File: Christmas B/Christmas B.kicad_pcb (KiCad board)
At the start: 2 copper layers, 80.1 x 92.6 mm, 38 parts, among them J1 LEFT, J2 RIGHT

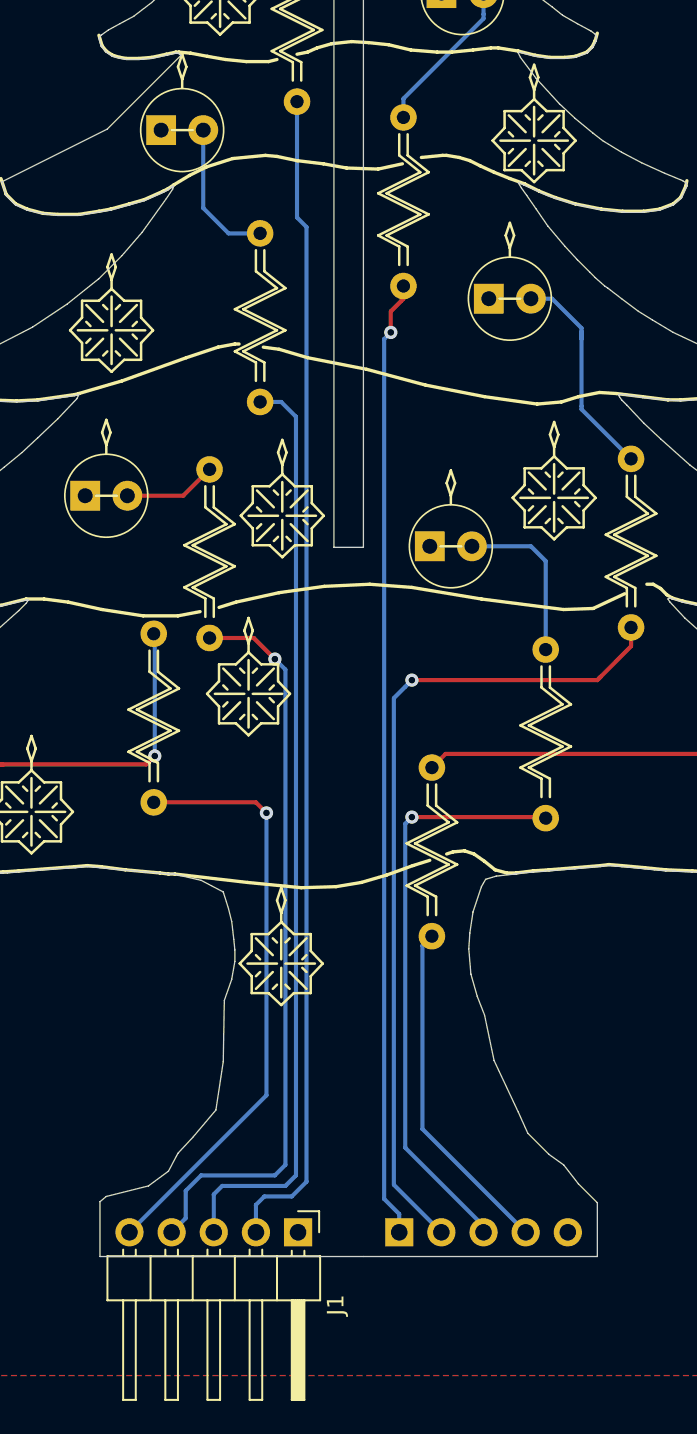
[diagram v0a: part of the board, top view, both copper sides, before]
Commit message: Make space at the bottom
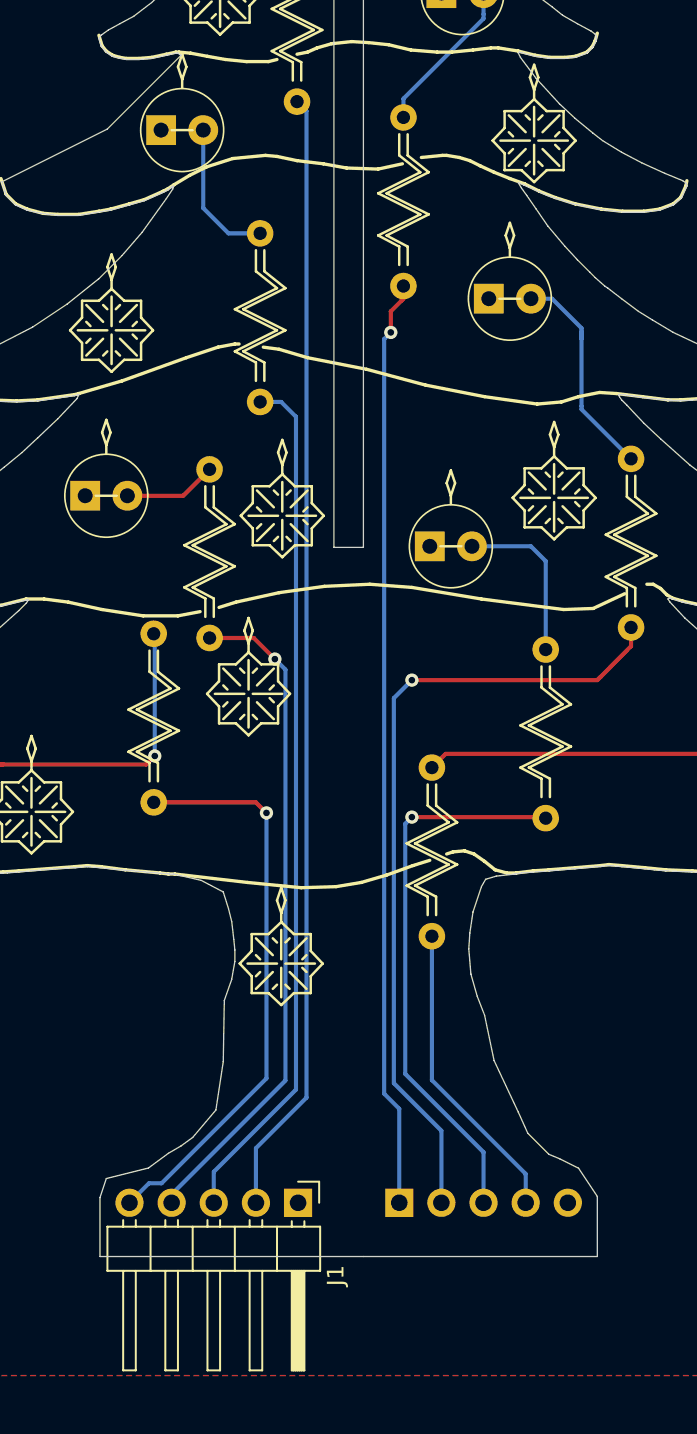
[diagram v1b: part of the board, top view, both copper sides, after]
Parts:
- moved J1 1.78 mm to (101.7, 148.3)
- moved J2 1.78 mm to (107.8, 148.3)
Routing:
- net Net-(J1-Pad4): track 44.7 -> 40.3 mm
- net Net-(J1-Pad3): track 56.0 -> 51.9 mm
- net Net-(J1-Pad2): track 70.6 -> 67.9 mm
- net Net-(J2-Pad4): track 20.7 -> 18.4 mm
- net Net-(J2-Pad3): track 35.2 -> 33.5 mm
- net Net-(J2-Pad2): track 50.3 -> 48.5 mm
- net Net-(J2-Pad1): track 57.9 -> 56.1 mm
- net Net-(J1-Pad5): track 35.7 -> 34.4 mm
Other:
- outline, holes or cut-outs redrawn

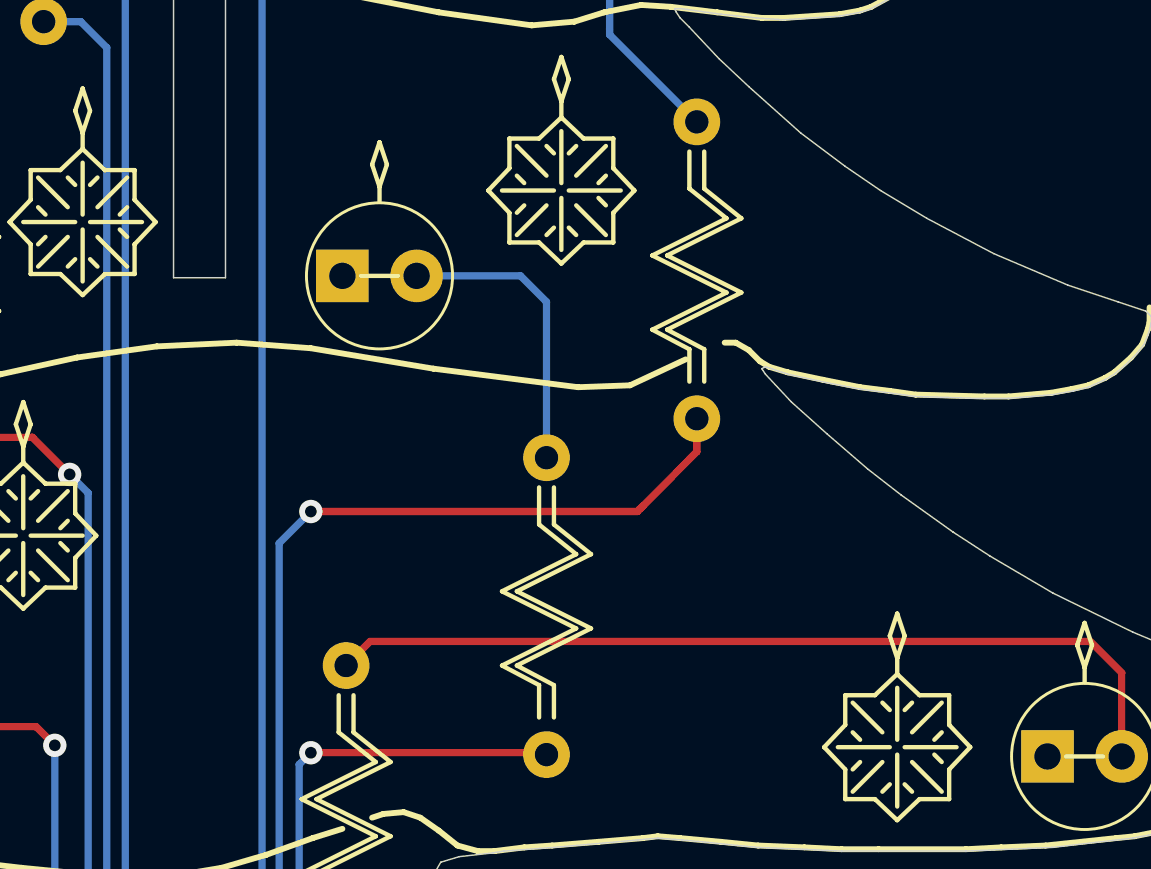
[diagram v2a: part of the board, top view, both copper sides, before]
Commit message: Added part designation to A/B
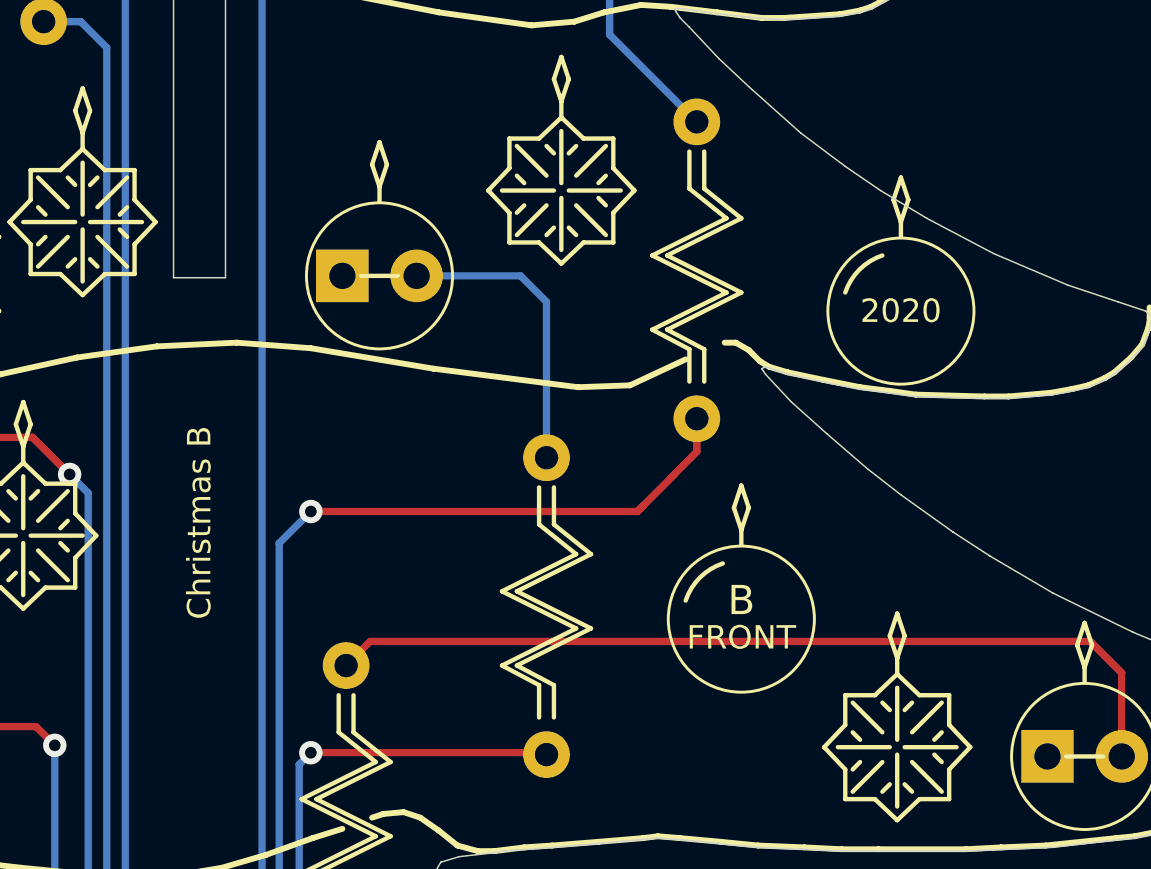
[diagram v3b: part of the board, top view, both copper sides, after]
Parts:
- added A?: Part A, christmas:ball, F.Cu at (127.5, 110.0)
- added A?: Part A, christmas:part_b, F.Cu at (122.0, 120.5)
- moved A? 7.12 mm to (131.4, 122.7)
- moved A? 0.83 mm to (110.0, 117.2)
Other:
- board text added: "Christmas B"
- board text added: "github.com/tebl"
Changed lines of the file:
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@@
   (general
     (thickness 1.6)
-    (drawings 789)
+    (drawings 791)
     (tracks 87)
     (zones 0)
-    (modules 38)
+    (modules 40)
     (nets 18)
   )
@@
     (add_net "Net-(J2-Pad4)")
   )
+  (module christmas:ball locked (layer F.Cu)
+    (at 127.508 109.982)
+    (descr "LED, diameter 5.0mm, 2 pins, http://cdn-reichelt.de/documents/datenblatt/A500/LL-504BC2E-009.pdf")
+    (tags "LED diameter 5.0mm 2 pins")
+    (fp_text reference A? (at -0.635 -3.81) (layer F.Fab) hide
+      (effects (font (size 1 1) (thickness 0.15)))
+    )
+    (fp_text value "Part A" (at 1.27 3.96) (layer F.Fab) hide
+      (effects (font (size 1 1) (thickness 0.15)))
+    )
+    (fp_text user 2020 (at 1.27 0) (layer F.SilkS)
+      (effects (font (size 0.8 0.8) (thickness 0.1)))
+    )
+    (fp_arc (start 1.27 0) (end 0.635001 -1.904999) (angle -53.13010235) (layer F.SilkS) (width 0.15))
+    (fp_line (start 1.524 -3.81) (end 1.27 -3.048) (layer F.SilkS) (width 0.15))
+    (fp_line (start 1.27 -4.572) (end 1.524 -3.81) (layer F.SilkS) (width 0.15))
+    (fp_line (start 1.016 -3.81) (end 1.27 -4.572) (layer F.SilkS) (width 0.15))
+    (fp_line (start 1.27 -3.048) (end 1.016 -3.81) (layer F.SilkS) (width 0.15))
+    (fp_line (start 1.27 -2.54) (end 1.27 -3.048) (layer F.SilkS) (width 0.15))
+    (fp_text user %R (at 3.81 -3.81) (layer F.Fab) hide
+      (effects (font (size 0.8 0.8) (thickness 0.2)))
+    )
+    (fp_line (start 4.5 -3.25) (end -1.95 -3.25) (layer F.CrtYd) (width 0.05))
+    (fp_line (start 4.5 3.25) (end 4.5 -3.25) (layer F.CrtYd) (width 0.05))
+    (fp_line (start -1.95 3.25) (end 4.5 3.25) (layer F.CrtYd) (width 0.05))
+    (fp_line (start -1.95 -3.25) (end -1.95 3.25) (layer F.CrtYd) (width 0.05))
+    (fp_line (start -1.23 -1.469694) (end -1.23 1.469694) (layer F.Fab) (width 0.1))
+    (fp_circle (center 1.27 0) (end 3.77 0) (layer F.SilkS) (width 0.1))
+    (fp_arc (start 1.27 0) (end -1.23 -1.469694) (angle 299.1) (layer F.Fab) (width 0.1))
+    (model ${KISYS3DMOD}/LEDs.3dshapes/LED_D5.0mm.wrl
+      (at (xyz 0 0 0))
+      (scale (xyz 0.393701 0.393701 0.393701))
+      (rotate (xyz 0 0 0))
+    )
+  )
+  (module christmas:part_b locked (layer F.Cu)
+    (at 122.047 120.523)
+    (descr "LED, diameter 5.0mm, 2 pins, http://cdn-reichelt.de/documents/datenblatt/A500/LL-504BC2E-009.pdf")
+    (tags "LED diameter 5.0mm 2 pins")
+    (fp_text reference A? (at -0.635 -3.81) (layer F.Fab) hide
+      (effects (font (size 1 1) (thickness 0.15)))
+    )
+    (fp_text value "Part A" (at 1.27 3.96) (layer F.Fab) hide
+      (effects (font (size 1 1) (thickness 0.15)))
+    )
+    (fp_text user BACK (at 1.27 0.635) (layer B.SilkS)
+      (effects (font (size 0.8 0.8) (thickness 0.1)) (justify mirror))
+    )
+    (fp_text user B (at 1.27 -0.635) (layer B.SilkS)
+      (effects (font (size 1 1) (thickness 0.15)) (justify mirror))
+    )
+    (fp_arc (start 1.270001 -0.000001) (end 3.175 -0.635) (angle -53.1) (layer B.SilkS) (width 0.15))
+    (fp_arc (start 1.27 0) (end 0.635001 -1.904999) (angle -53.13010235) (layer F.SilkS) (width 0.15))
+    (fp_text user FRONT (at 1.27 0.635) (layer F.SilkS)
+      (effects (font (size 0.8 0.8) (thickness 0.1)))
+    )
+    (fp_text user B (at 1.27 -0.635) (layer F.SilkS)
+      (effects (font (size 1 1) (thickness 0.15)))
+    )
+    (fp_circle (center 1.27 0) (end -1.23 0) (layer B.SilkS) (width 0.1))
+    (fp_line (start 1.27 -4.572) (end 1.016 -3.81) (layer B.SilkS) (width 0.15))
+    (fp_line (start 1.016 -3.81) (end 1.27 -3.048) (layer B.SilkS) (width 0.15))
+    (fp_line (start 1.27 -3.048) (end 1.524 -3.81) (layer B.SilkS) (width 0.15))
+    (fp_line (start 1.524 -3.81) (end 1.27 -4.572) (layer B.SilkS) (width 0.15))
+    (fp_line (start 1.27 -2.54) (end 1.27 -3.048) (layer B.SilkS) (width 0.15))
+    (fp_line (start 1.524 -3.81) (end 1.27 -3.048) (layer F.SilkS) (width 0.15))
+    (fp_line (start 1.27 -4.572) (end 1.524 -3.81) (layer F.SilkS) (width 0.15))
+    (fp_line (start 1.016 -3.81) (end 1.27 -4.572) (layer F.SilkS) (width 0.15))
+    (fp_line (start 1.27 -3.048) (end 1.016 -3.81) (layer F.SilkS) (width 0.15))
+    (fp_line (start 1.27 -2.54) (end 1.27 -3.048) (layer F.SilkS) (width 0.15))
+    (fp_text user %R (at 3.81 -3.81) (layer F.Fab) hide
+      (effects (font (size 0.8 0.8) (thickness 0.2)))
+    )
+    (fp_line (start 4.5 -3.25) (end -1.95 -3.25) (layer F.CrtYd) (width 0.05))
+    (fp_line (start 4.5 3.25) (end 4.5 -3.25) (layer F.CrtYd) (width 0.05))
+    (fp_line (start -1.95 3.25) (end 4.5 3.25) (layer F.CrtYd) (width 0.05))
+    (fp_line (start -1.95 -3.25) (end -1.95 3.25) (layer F.CrtYd) (width 0.05))
+    (fp_line (start -1.23 -1.469694) (end -1.23 1.469694) (layer F.Fab) (width 0.1))
+    (fp_circle (center 1.27 0) (end 3.77 0) (layer F.SilkS) (width 0.1))
+    (fp_arc (start 1.27 0) (end -1.23 -1.469694) (angle 299.1) (layer F.Fab) (width 0.1))
+    (model ${KISYS3DMOD}/LEDs.3dshapes/LED_D5.0mm.wrl
+      (at (xyz 0 0 0))
+      (scale (xyz 0.393701 0.393701 0.393701))
+      (rotate (xyz 0 0 0))
+    )
+  )
   (module christmas:star locked (layer F.Cu)
     (at 99.441 133.9215)
@@
   )
   (module christmas:star (layer B.Cu)
-    (at 109.22 117.5385 180)
+    (at 109.982 117.221 180)
     (descr "LED, diameter 5.0mm, 2 pins, http://cdn-reichelt.de/documents/datenblatt/A500/LL-504BC2E-009.pdf")
     (tags "LED diameter 5.0mm 2 pins")
@@
   )
   (module christmas:star locked (layer B.Cu)
-    (at 124.587 120.777 180)
+    (at 131.445 122.682 180)
     (descr "LED, diameter 5.0mm, 2 pins, http://cdn-reichelt.de/documents/datenblatt/A500/LL-504BC2E-009.pdf")
     (tags "LED diameter 5.0mm 2 pins")
@@
     )
   )
+  (gr_text github.com/tebl (at 104.775 116.967 90) (layer B.SilkS)
+    (effects (font (size 0.8 0.8) (thickness 0.1)) (justify mirror))
+  )
+  (gr_text "Christmas B" (at 104.775 117.221 90) (layer F.SilkS)
+    (effects (font (size 0.8 0.8) (thickness 0.1)))
+  )
   (gr_line (start 109.9185 86.233) (end 108.077 85.979) (layer B.SilkS) (width 0.2))
